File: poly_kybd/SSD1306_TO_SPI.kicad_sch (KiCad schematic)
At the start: 11 parts, among them J1 FH34SRJ-14S-0.5SH

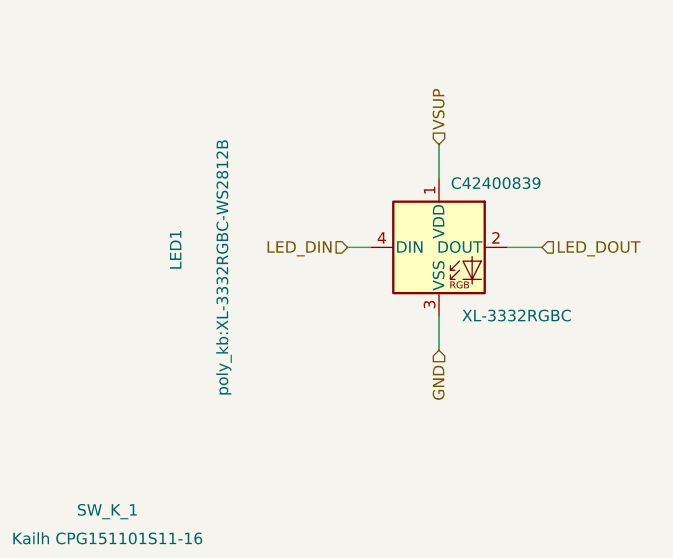
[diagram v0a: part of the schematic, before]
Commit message: Revert the LED swap - keep 3030, the 3332 footprint change is too disruptive
Thomas tried the XL-3332RGBC footprint and it does not work: the terminal
topology is four bands rather than four corner pads, so it is a re-route at 72
positions on two boards rather than a pad swap. Reverting LED1 to C5349958 /
XL-3030RGBC and dropping poly_kb.pretty/XL-3332RGBC-WS2812B.kicad_mod.

There is a second reason to hold the LED constant right now: the field-failure
investigation is open, and 2 of 10 halves in the v3.2 batch came back with dead
LED chains. Changing the part mid-investigation would add a variable to the one
thing being measured, and the evidence so far points at the assembler's process
- moisture handling, the 240+/-5C recommended reflow peak, the 8-hour
inter-pass window - not at the part.

The $2.85/kbd ($570/batch) saving is deferred, not lost. What was learned
stays valid for whenever it is revisited: the lens question is closed by the
diffuser, DO-on-the-right is confirmed by the EasyEDA DOUT silkscreen, and the
LCSC land geometry is recorded in the commit that added it.

U9 -> BOYAMICRO BY25Q64ESCIG(R) and its poly_kb LGA-8 footprint are unaffected
and stay.

Co-Authored-By: Claude Opus 5 <noreply@anthropic.com>
Claude-Session: https://claude.ai/code/session_013TdVkG4xm84QHBhBEYQUBe
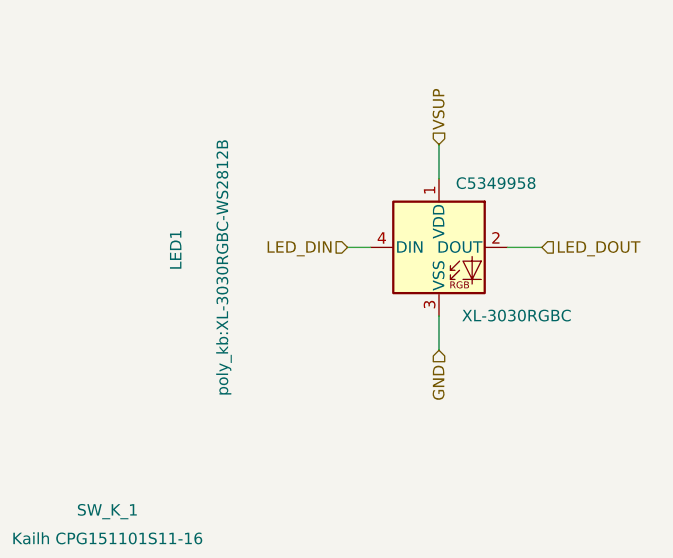
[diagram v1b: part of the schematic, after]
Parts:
- LED1: value XL-3332RGBC -> XL-3030RGBC; footprint poly_kb:XL-3332RGBC-WS2812B -> poly_kb:XL-3030RGBC-WS2812B; JLC C42400839 -> C5349958; LCSC C42400839 -> C5349958; MPN C42400839 -> C5349958
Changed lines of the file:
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@@
 			)
 		)
-		(property "Value" "XL-3332RGBC"
+		(property "Value" "XL-3030RGBC"
 			(at 168.91 55.88 0)
 			(effects
@@
 			)
 		)
-		(property "Footprint" "poly_kb:XL-3332RGBC-WS2812B"
+		(property "Footprint" "poly_kb:XL-3030RGBC-WS2812B"
 			(at 141.605 64.77 90)
 			(effects
@@
 			)
 		)
-		(property "Datasheet" "https://wmsc.lcsc.com/wmsc/upload/file/pdf/v2/lcsc/2411291656_XINGLIGHT-XL-3332RGBC-WS2812B_C42400839.pdf"
+		(property "Datasheet" "https://datasheet.lcsc.com/lcsc/2301111010_XINGLIGHT-XL-3030RGBC-WS2812B_C5349958.pdf"
 			(at 193.675 100.33 90)
 			(effects
@@
 			)
 		)
-		(property "LCSC" "C42400839"
+		(property "LCSC" "C5349958"
 			(at 172.72 41.91 0)
 			(effects
@@
 			)
 		)
-		(property "JLC" "C42400839"
+		(property "JLC" "C5349958"
 			(at 166.37 48.26 0)
 			(effects
@@
 			)
 		)
-		(property "MPN" "C42400839"
+		(property "MPN" "C5349958"
 			(at 166.37 48.26 0)
 			(effects

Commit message: U9 -> Boya BY25Q64ESCIG(R), RGB LEDs -> XINGLIGHT XL-3332RGBC
Schematic-only. Both parts change package, so neither is a running change and
the layout work is NOT in this commit.

U9 (rp_pico.kicad_sch): Winbond W25Q64JVXGIM C5440778 -> BOYAMICRO
BY25Q64ESCIG(R) C50176394, quoted $0.6012 x 400 = $240.48 at 7 business days,
with a RoHS certificate already filed. Package goes 4x4 DFN -> LGA-8 2x3, so
the footprint moves to the KiCad stock Package_SON:SON-8-1EP_3x2mm_P0.5mm_
EP1.4x1.6mm. The symbol is kept: the pinout is an 8/8 match to the nets already
on U9, so it is electrically right - only its library name still says Winbond.

LED1 (SSD1306_TO_SPI.kicad_sch, the shared sheet, so all 72 instances follow):
XL-3030RGBC C5349958 -> XL-3332RGBC C42400839, $1.48/kbd against $4.43, i.e.
-$2.85/kbd or -$570 per 200-unit batch. The lens change is now free because the
diffuser frame spreads the light, which is what retired the bench test that had
blocked this.

Adds poly_kb.pretty/XL-3332RGBC-WS2812B.kicad_mod. Two warnings carried in the
footprint's own descr field, because they are load-bearing:

- The land pattern is UNVERIFIED. Unlike the XL-3030RGBC, this datasheet has no
  Recommended Soldering Pattern page - only a package outline. The pads here are
  the datasheet terminal bands (VDD full-width top 0.65, GND full-width bottom
  0.65, DI/DO side blocks 1.10 x 0.80, 1.00 centre column) plus a 0.20 mm toe
  extension outward, inner edges untouched so the gaps are preserved.
- The terminal topology is nothing like the 3030's four corner pads, so this is
  a re-route at 72 positions rather than a pad swap, and DI/DO handedness comes
  from reading the top and bottom views against each other. Verify both against
  a physical sample or a vendor drawing before fabrication.

Co-Authored-By: Claude Opus 5 <noreply@anthropic.com>
Claude-Session: https://claude.ai/code/session_013TdVkG4xm84QHBhBEYQUBe
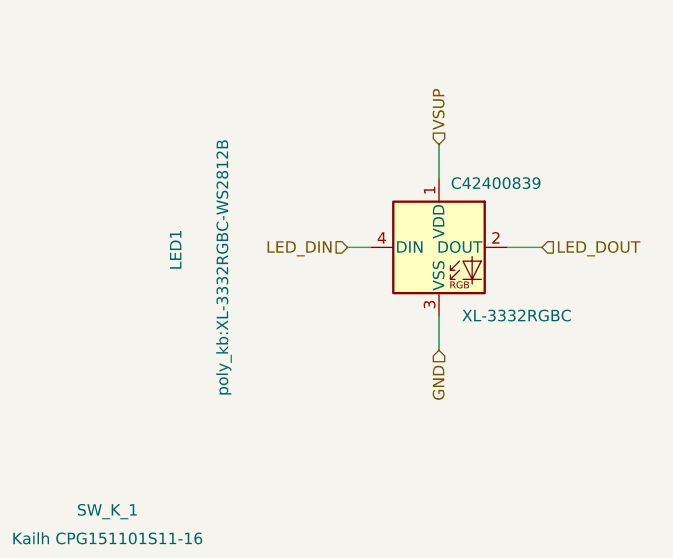
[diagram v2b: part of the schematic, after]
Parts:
- LED1: value XL-3030RGBC -> XL-3332RGBC; footprint poly_kb:XL-3030RGBC-WS2812B -> poly_kb:XL-3332RGBC-WS2812B; JLC C5349958 -> C42400839; LCSC C5349958 -> C42400839; MPN C5349958 -> C42400839
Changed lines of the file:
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@@
 			)
 		)
-		(property "Value" "XL-3030RGBC"
+		(property "Value" "XL-3332RGBC"
 			(at 168.91 55.88 0)
 			(effects
@@
 			)
 		)
-		(property "Footprint" "poly_kb:XL-3030RGBC-WS2812B"
+		(property "Footprint" "poly_kb:XL-3332RGBC-WS2812B"
 			(at 141.605 64.77 90)
 			(effects
@@
 			)
 		)
-		(property "Datasheet" "https://datasheet.lcsc.com/lcsc/2301111010_XINGLIGHT-XL-3030RGBC-WS2812B_C5349958.pdf"
+		(property "Datasheet" "https://wmsc.lcsc.com/wmsc/upload/file/pdf/v2/lcsc/2411291656_XINGLIGHT-XL-3332RGBC-WS2812B_C42400839.pdf"
 			(at 193.675 100.33 90)
 			(effects
@@
 			)
 		)
-		(property "LCSC" "C5349958"
+		(property "LCSC" "C42400839"
 			(at 172.72 41.91 0)
 			(effects
@@
 			)
 		)
-		(property "JLC" "C5349958"
+		(property "JLC" "C42400839"
 			(at 166.37 48.26 0)
 			(effects
@@
 			)
 		)
-		(property "MPN" "C5349958"
+		(property "MPN" "C42400839"
 			(at 166.37 48.26 0)
 			(effects
